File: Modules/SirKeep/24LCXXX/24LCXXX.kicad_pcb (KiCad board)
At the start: 2 copper layers, 18 x 16.8 mm, 17 parts, among them J1 Conn_01x05

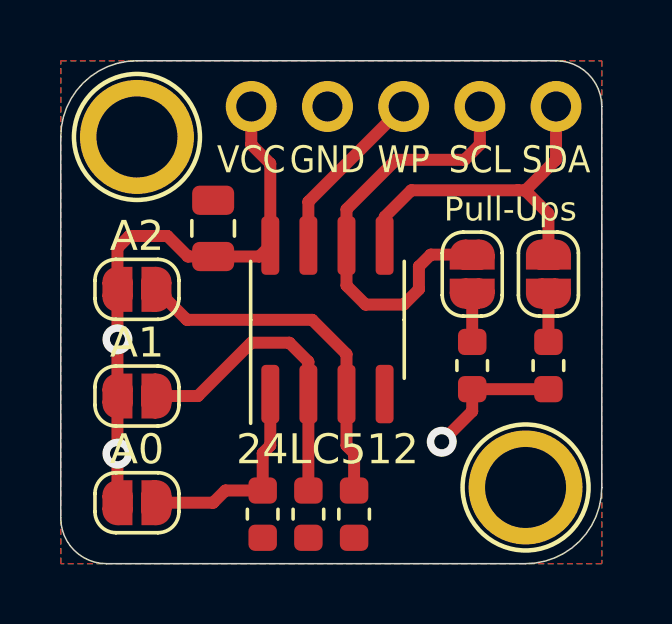
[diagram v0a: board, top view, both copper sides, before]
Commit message: 24LCXXX Added in place of 24512
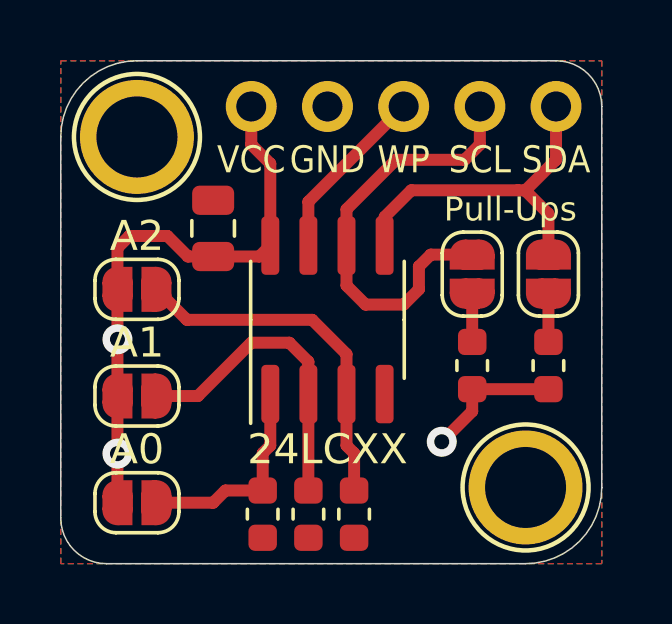
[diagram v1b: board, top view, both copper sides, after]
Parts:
- G***: footprint logo:logo76x107 -> logo:logo63x89
- moved G*** 2.32 mm to (58.9, 46.7)
- moved G*** 0.38 mm to (53.5, 44.8)
- renumbered 24LC512 to 24LCXX
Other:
- board text added: "128kB"
- board text added: "16kB"
- board text added: "24LCXXX I2C EEPROM"
- board text added: "32kB"
- board text added: "64kB"
- board text added: "8kB"
- board text removed: "24LC512 Board I2C EEPROM 64kBytes"
